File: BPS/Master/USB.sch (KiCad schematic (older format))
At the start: 8 parts, among them J11 USB_B_Micro, U15 CP2102N-A01-GQFN24

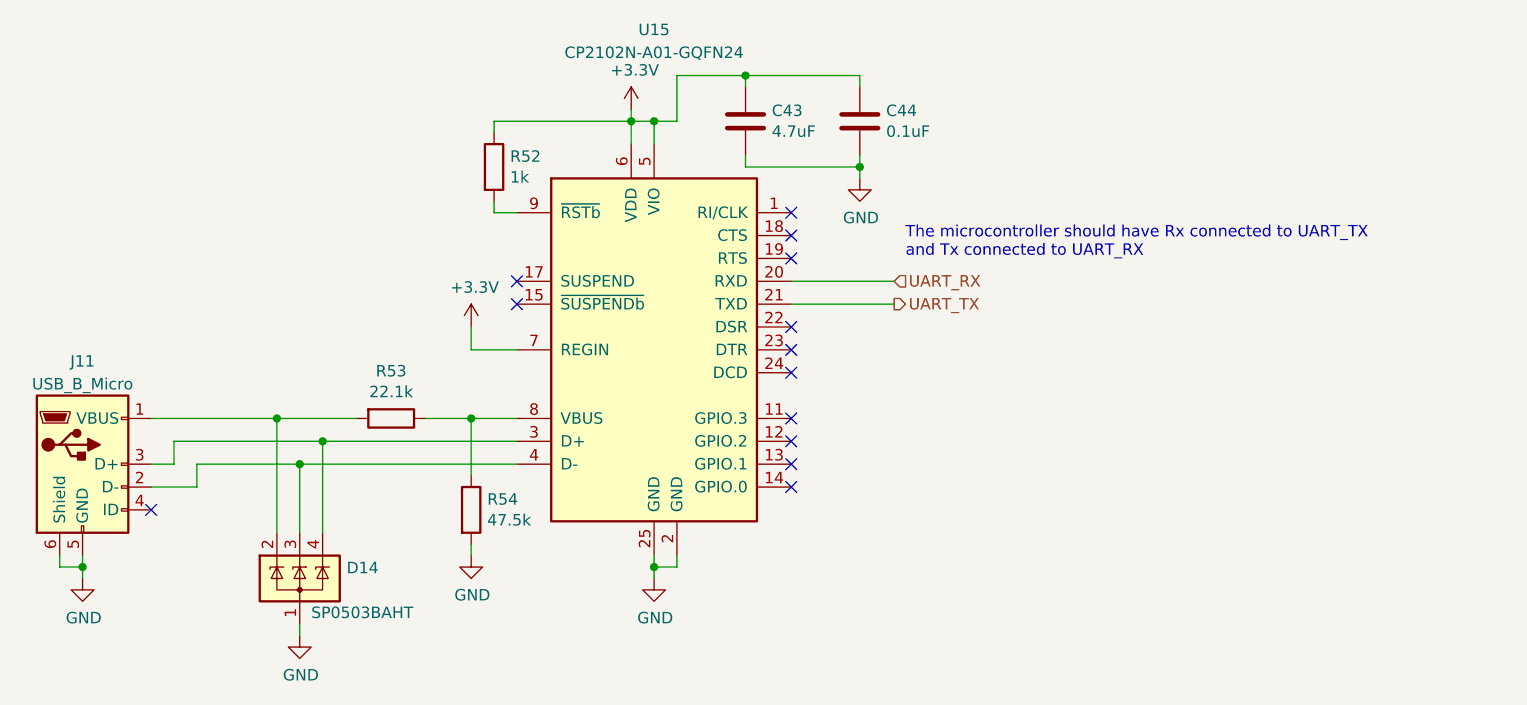
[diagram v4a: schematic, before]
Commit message: Creates fan brd interface schematics and updates symbols/footprints related to the leader board
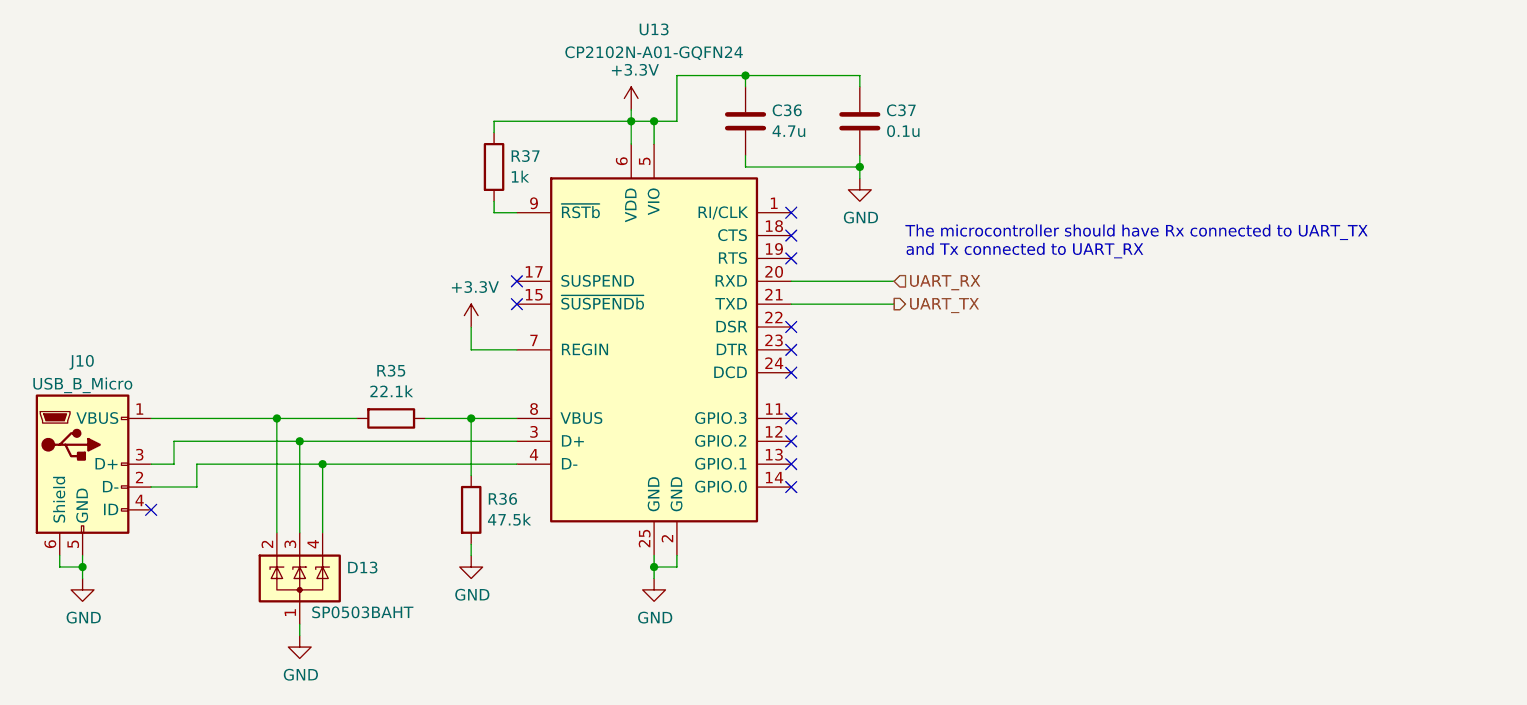
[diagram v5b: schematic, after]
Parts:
- C36: renamed from C43; value 4.7uF -> 4.7u
- C37: renamed from C44; value 0.1uF -> 0.1u
- renumbered D14 to D13, J11 to J10, R53 to R35, R54 to R36, R52 to R37, U15 to U13
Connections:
- net at J10.3 (D+), U13.3 (D+): now also D13.3 (K); no longer D13.4 (K)
- net at J10.2 (D-), U13.4 (D-): now also D13.4 (K); no longer D13.3 (K)
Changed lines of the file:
@@
 $Descr A4 11693 8268
 encoding utf-8
-Sheet 11 10
+Sheet 9 10
 Title ""
 Date ""
@@
 $EndDescr
 $Comp
-L Interface_USB:CP2102N-A01-GQFN24 U15
+L Interface_USB:CP2102N-A01-GQFN24 U13
 U 1 1 5C4963B2
 P 5500 3800
-F 0 "U15" H 5500 5200 50  0000 C CNN
+F 0 "U13" H 5500 5200 50  0000 C CNN
 F 1 "CP2102N-A01-GQFN24" H 5500 5100 50  0000 C CNN
 F 2 "Package_DFN_QFN:QFN-24-1EP_4x4mm_P0.5mm_EP2.6x2.6mm" H 5950 3000 50  0001 L CNN
@@
 $EndComp
 $Comp
-L Connector:USB_B_Micro J11
+L Connector:USB_B_Micro J10
 U 1 1 5C4964BB
 P 3000 4300
-F 0 "J11" H 3000 4750 50  0000 C CNN
+F 0 "J10" H 3000 4750 50  0000 C CNN
 F 1 "USB_B_Micro" H 3000 4650 50  0000 C CNN
 F 2 "Connector_USB:USB_Micro-B_Molex-105017-0001" H 3150 4250 50  0001 C CNN
@@
 	3500 4400 3500 4300
 $Comp
-L power:GND #PWR087
+L power:GND #PWR071
 U 1 1 5C4965DF
 P 3000 4800
-F 0 "#PWR087" H 3000 4550 50  0001 C CNN
+F 0 "#PWR071" H 3000 4550 50  0001 C CNN
 F 1 "GND" H 3005 4627 50  0000 C CNN
 F 2 "" H 3000 4800 50  0001 C CNN
@@
 Connection ~ 3000 4750
 $Comp
-L power:GND #PWR088
+L power:GND #PWR076
 U 1 1 5C4966CF
 P 5500 4800
-F 0 "#PWR088" H 5500 4550 50  0001 C CNN
+F 0 "#PWR076" H 5500 4550 50  0001 C CNN
 F 1 "GND" H 5505 4627 50  0000 C CNN
 F 2 "" H 5500 4800 50  0001 C CNN
@@
 	5500 4750 5500 4800
 $Comp
-L Power_Protection:SP0503BAHT D14
+L Power_Protection:SP0503BAHT D13
 U 1 1 5C496C9B
 P 3950 4800
-F 0 "D14" H 4155 4846 50  0000 L CNN
+F 0 "D13" H 4155 4846 50  0000 L CNN
 F 1 "SP0503BAHT" H 4000 4650 50  0000 L CNN
 F 2 "Package_TO_SOT_SMD:SOT-143" H 4175 4750 50  0001 L CNN
@@
 $EndComp
 $Comp
-L power:GND #PWR089
+L power:GND #PWR072
 U 1 1 5C497074
 P 3950 5050
-F 0 "#PWR089" H 3950 4800 50  0001 C CNN
+F 0 "#PWR072" H 3950 4800 50  0001 C CNN
 F 1 "GND" H 3955 4877 50  0000 C CNN
 F 2 "" H 3950 5050 50  0001 C CNN
@@
 	3850 4600 3850 4100
 $Comp
-L Device:R R54
+L Device:R R36
 U 1 1 5C497DB9
 P 4700 4500
-F 0 "R54" H 4770 4546 50  0000 L CNN
+F 0 "R36" H 4770 4546 50  0000 L CNN
 F 1 "47.5k" H 4770 4455 50  0000 L CNN
 F 2 "Resistor_SMD:R_0805_2012Metric" V 4630 4500 50  0001 C CNN
@@
 $EndComp
 $Comp
-L Device:R R53
+L Device:R R35
 U 1 1 5C497DDB
 P 4350 4100
-F 0 "R53" V 4143 4100 50  0000 C CNN
+F 0 "R35" V 4143 4100 50  0000 C CNN
 F 1 "22.1k" V 4234 4100 50  0000 C CNN
 F 2 "Resistor_SMD:R_0805_2012Metric" V 4280 4100 50  0001 C CNN
@@
 	4200 4100 3850 4100
 $Comp
-L power:GND #PWR086
+L power:GND #PWR074
 U 1 1 5C498DBE
 P 4700 4700
-F 0 "#PWR086" H 4700 4450 50  0001 C CNN
+F 0 "#PWR074" H 4700 4450 50  0001 C CNN
 F 1 "GND" H 4705 4527 50  0000 C CNN
 F 2 "" H 4700 4700 50  0001 C CNN
@@
 	4700 4700 4700 4650
 $Comp
-L power:+3.3V #PWR083
+L power:+3.3V #PWR075
 U 1 1 5C499E7D
 P 5400 2750
-F 0 "#PWR083" H 5400 2600 50  0001 C CNN
+F 0 "#PWR075" H 5400 2600 50  0001 C CNN
 F 1 "+3.3V" H 5415 2923 50  0000 C CNN
 F 2 "" H 5400 2750 50  0001 C CNN
@@
 Connection ~ 5400 2800
 $Comp
-L Device:R R52
+L Device:R R37
 U 1 1 5C49B01B
 P 4800 3000
-F 0 "R52" H 4870 3046 50  0000 L CNN
+F 0 "R37" H 4870 3046 50  0000 L CNN
 F 1 "1k" H 4870 2955 50  0000 L CNN
 F 2 "Resistor_SMD:R_0805_2012Metric" V 4730 3000 50  0001 C CNN
@@
 	4800 2800 5400 2800
 $Comp
-L Device:C C43
+L Device:C C36
 U 1 1 5C49CC52
 P 5900 2800
-F 0 "C43" H 6015 2846 50  0000 L CNN
-F 1 "4.7uF" H 6015 2755 50  0000 L CNN
+F 0 "C36" H 6015 2846 50  0000 L CNN
+F 1 "4.7u" H 6015 2755 50  0000 L CNN
 F 2 "Capacitor_SMD:C_0805_2012Metric" H 5938 2650 50  0001 C CNN
 F 3 "~" H 5900 2800 50  0001 C CNN
@@
 NoConn ~ 6100 4400
 $Comp
-L power:+3.3V #PWR085
+L power:+3.3V #PWR073
 U 1 1 5C4A2CBF
 P 4700 3700
-F 0 "#PWR085" H 4700 3550 50  0001 C CNN
+F 0 "#PWR073" H 4700 3550 50  0001 C CNN
 F 1 "+3.3V" H 4715 3873 50  0000 C CNN
 F 2 "" H 4700 3700 50  0001 C CNN
@@
 	4700 3800 4900 3800
 $Comp
-L Device:C C44
+L Device:C C37
 U 1 1 5C4A4791
 P 6400 2800
-F 0 "C44" H 6515 2846 50  0000 L CNN
-F 1 "0.1uF" H 6515 2755 50  0000 L CNN
+F 0 "C37" H 6515 2846 50  0000 L CNN
+F 1 "0.1u" H 6515 2755 50  0000 L CNN
 F 2 "Capacitor_SMD:C_0805_2012Metric" H 6438 2650 50  0001 C CNN
 F 3 "~" H 6400 2800 50  0001 C CNN
@@
 $EndComp
 $Comp
-L power:GND #PWR084
+L power:GND #PWR077
 U 1 1 5C4A4BE4
 P 6400 3050
-F 0 "#PWR084" H 6400 2800 50  0001 C CNN
+F 0 "#PWR077" H 6400 2800 50  0001 C CNN
 F 1 "GND" H 6405 2877 50  0000 C CNN
 F 2 "" H 6400 3050 50  0001 C CNN
@@
 	3300 4100 3850 4100
 Wire Wire Line
-	3500 4300 3950 4300
-Wire Wire Line
-	3400 4200 4050 4200
-Wire Wire Line
-	4050 4600 4050 4200
-Connection ~ 4050 4200
-Wire Wire Line
-	4050 4200 4900 4200
-Wire Wire Line
-	3950 4600 3950 4300
-Connection ~ 3950 4300
-Wire Wire Line
-	3950 4300 4900 4300
+	3400 4200 3950 4200
+Wire Wire Line
+	3500 4300 4050 4300
+Wire Wire Line
+	4050 4600 4050 4300
+Connection ~ 4050 4300
+Wire Wire Line
+	4050 4300 4900 4300
+Wire Wire Line
+	3950 4200 3950 4600
+Connection ~ 3950 4200
+Wire Wire Line
+	3950 4200 4900 4200
 $EndSCHEMATC

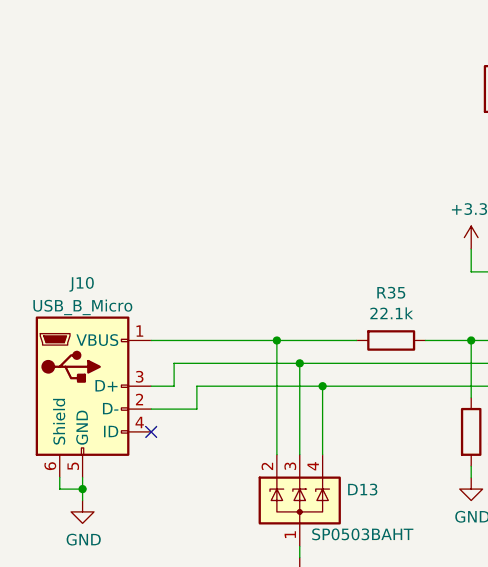
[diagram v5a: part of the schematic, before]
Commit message: Finishes schematics for bps leader board
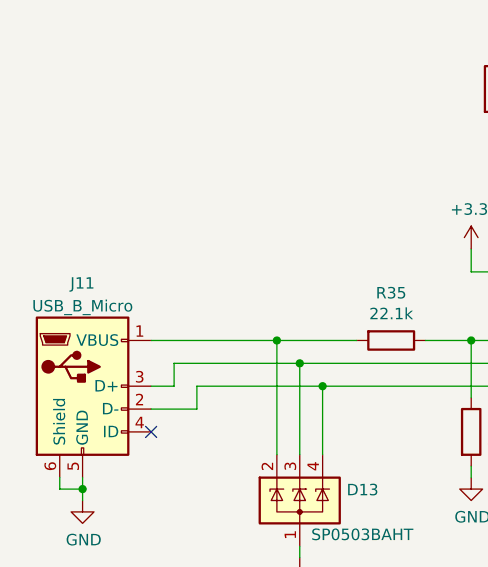
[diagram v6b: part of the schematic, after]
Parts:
- renumbered J10 to J11
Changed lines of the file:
@@
 $Descr A4 11693 8268
 encoding utf-8
-Sheet 9 10
+Sheet 9 11
 Title ""
 Date ""
@@
 $EndComp
 $Comp
-L Connector:USB_B_Micro J10
+L Connector:USB_B_Micro J11
 U 1 1 5C4964BB
 P 3000 4300
-F 0 "J10" H 3000 4750 50  0000 C CNN
+F 0 "J11" H 3000 4750 50  0000 C CNN
 F 1 "USB_B_Micro" H 3000 4650 50  0000 C CNN
 F 2 "Connector_USB:USB_Micro-B_Molex-105017-0001" H 3150 4250 50  0001 C CNN
@@
 	3500 4400 3500 4300
 $Comp
-L power:GND #PWR071
+L power:GND #PWR074
 U 1 1 5C4965DF
 P 3000 4800
-F 0 "#PWR071" H 3000 4550 50  0001 C CNN
+F 0 "#PWR074" H 3000 4550 50  0001 C CNN
 F 1 "GND" H 3005 4627 50  0000 C CNN
 F 2 "" H 3000 4800 50  0001 C CNN
@@
 Connection ~ 3000 4750
 $Comp
-L power:GND #PWR076
+L power:GND #PWR079
 U 1 1 5C4966CF
 P 5500 4800
-F 0 "#PWR076" H 5500 4550 50  0001 C CNN
+F 0 "#PWR079" H 5500 4550 50  0001 C CNN
 F 1 "GND" H 5505 4627 50  0000 C CNN
 F 2 "" H 5500 4800 50  0001 C CNN
@@
 $EndComp
 $Comp
-L power:GND #PWR072
+L power:GND #PWR075
 U 1 1 5C497074
 P 3950 5050
-F 0 "#PWR072" H 3950 4800 50  0001 C CNN
+F 0 "#PWR075" H 3950 4800 50  0001 C CNN
 F 1 "GND" H 3955 4877 50  0000 C CNN
 F 2 "" H 3950 5050 50  0001 C CNN
@@
 	4200 4100 3850 4100
 $Comp
-L power:GND #PWR074
+L power:GND #PWR077
 U 1 1 5C498DBE
 P 4700 4700
-F 0 "#PWR074" H 4700 4450 50  0001 C CNN
+F 0 "#PWR077" H 4700 4450 50  0001 C CNN
 F 1 "GND" H 4705 4527 50  0000 C CNN
 F 2 "" H 4700 4700 50  0001 C CNN
@@
 	4700 4700 4700 4650
 $Comp
-L power:+3.3V #PWR075
+L power:+3.3V #PWR078
 U 1 1 5C499E7D
 P 5400 2750
-F 0 "#PWR075" H 5400 2600 50  0001 C CNN
+F 0 "#PWR078" H 5400 2600 50  0001 C CNN
 F 1 "+3.3V" H 5415 2923 50  0000 C CNN
 F 2 "" H 5400 2750 50  0001 C CNN
@@
 NoConn ~ 6100 4400
 $Comp
-L power:+3.3V #PWR073
+L power:+3.3V #PWR076
 U 1 1 5C4A2CBF
 P 4700 3700
-F 0 "#PWR073" H 4700 3550 50  0001 C CNN
+F 0 "#PWR076" H 4700 3550 50  0001 C CNN
 F 1 "+3.3V" H 4715 3873 50  0000 C CNN
 F 2 "" H 4700 3700 50  0001 C CNN
@@
 $EndComp
 $Comp
-L power:GND #PWR077
+L power:GND #PWR080
 U 1 1 5C4A4BE4
 P 6400 3050
-F 0 "#PWR077" H 6400 2800 50  0001 C CNN
+F 0 "#PWR080" H 6400 2800 50  0001 C CNN
 F 1 "GND" H 6405 2877 50  0000 C CNN
 F 2 "" H 6400 3050 50  0001 C CNN
